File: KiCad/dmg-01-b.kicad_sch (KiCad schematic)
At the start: 64 parts, among them CN1 SCREEN, CN2 CART, CN3 EXT, CN4 AUDIO, CN5 POWER, CN6 BATTERY, P1 CART SHIELD GND PADS, P2 GND PAD, P3 GND PAD, P4 GND PAD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

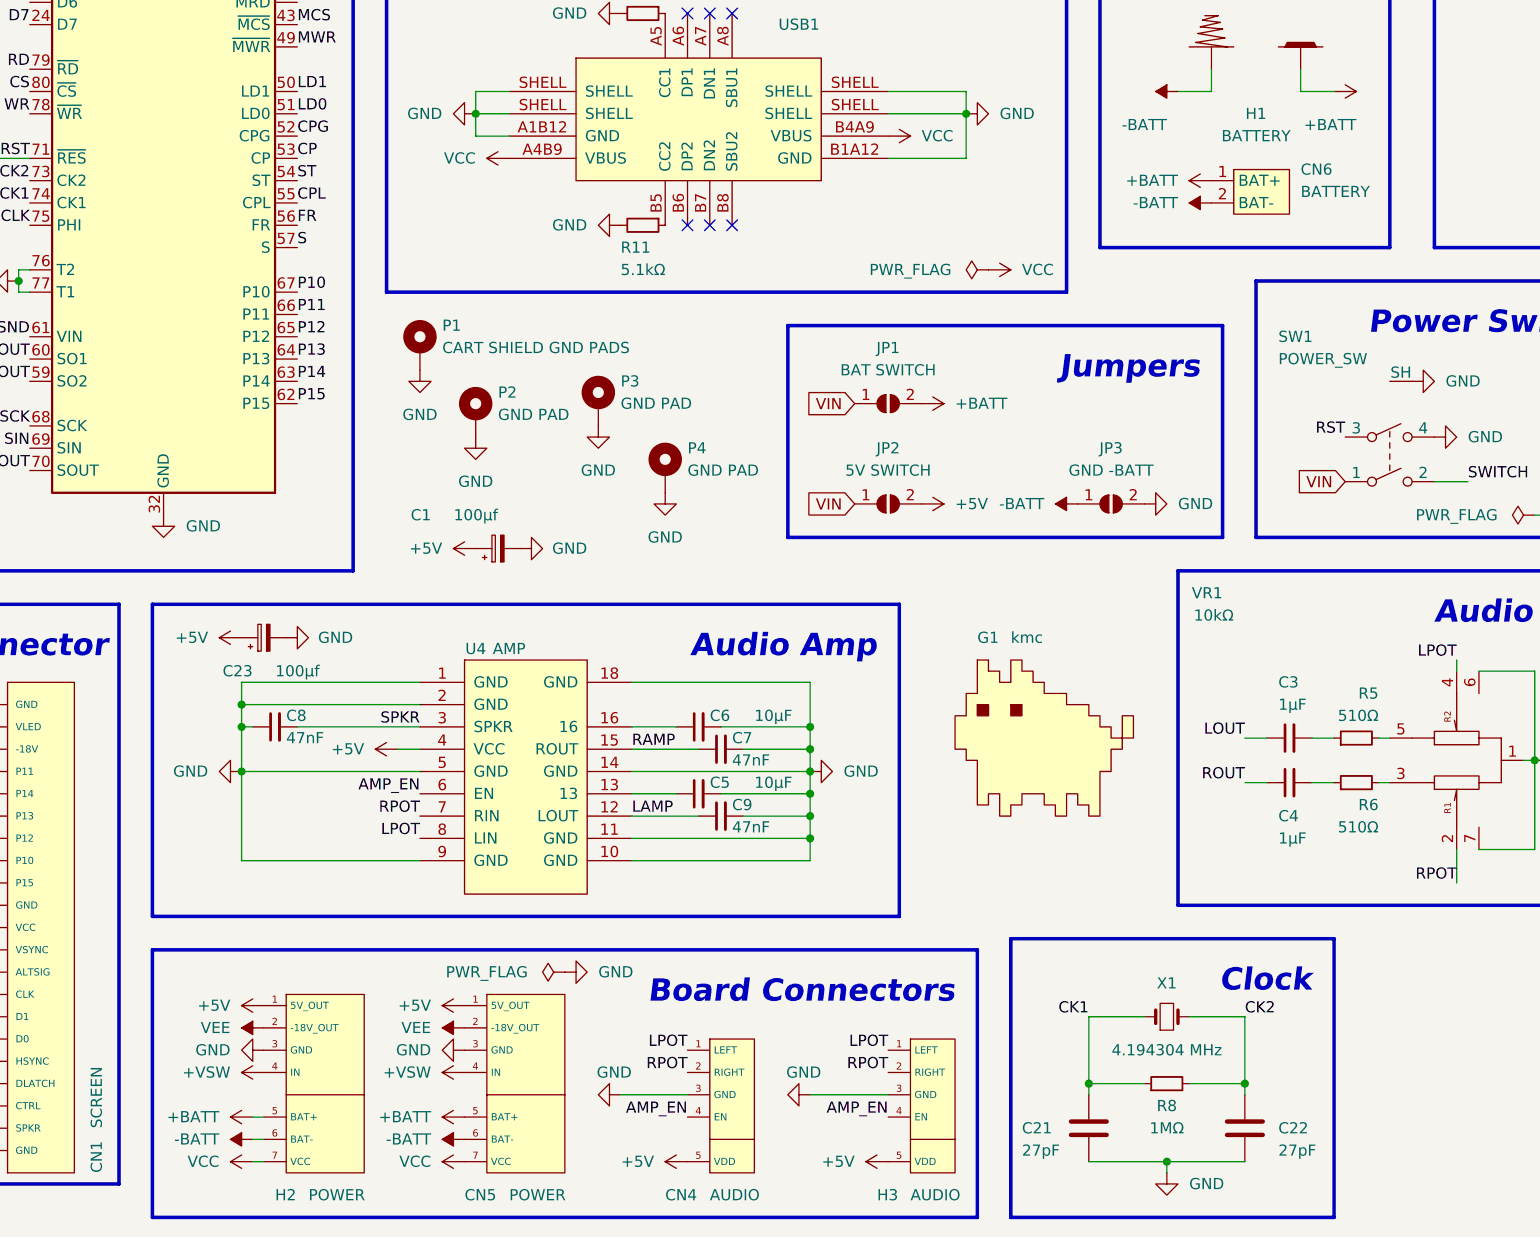
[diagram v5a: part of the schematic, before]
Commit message: fixed battery connector (!) less stupid routing in some areas minor changes
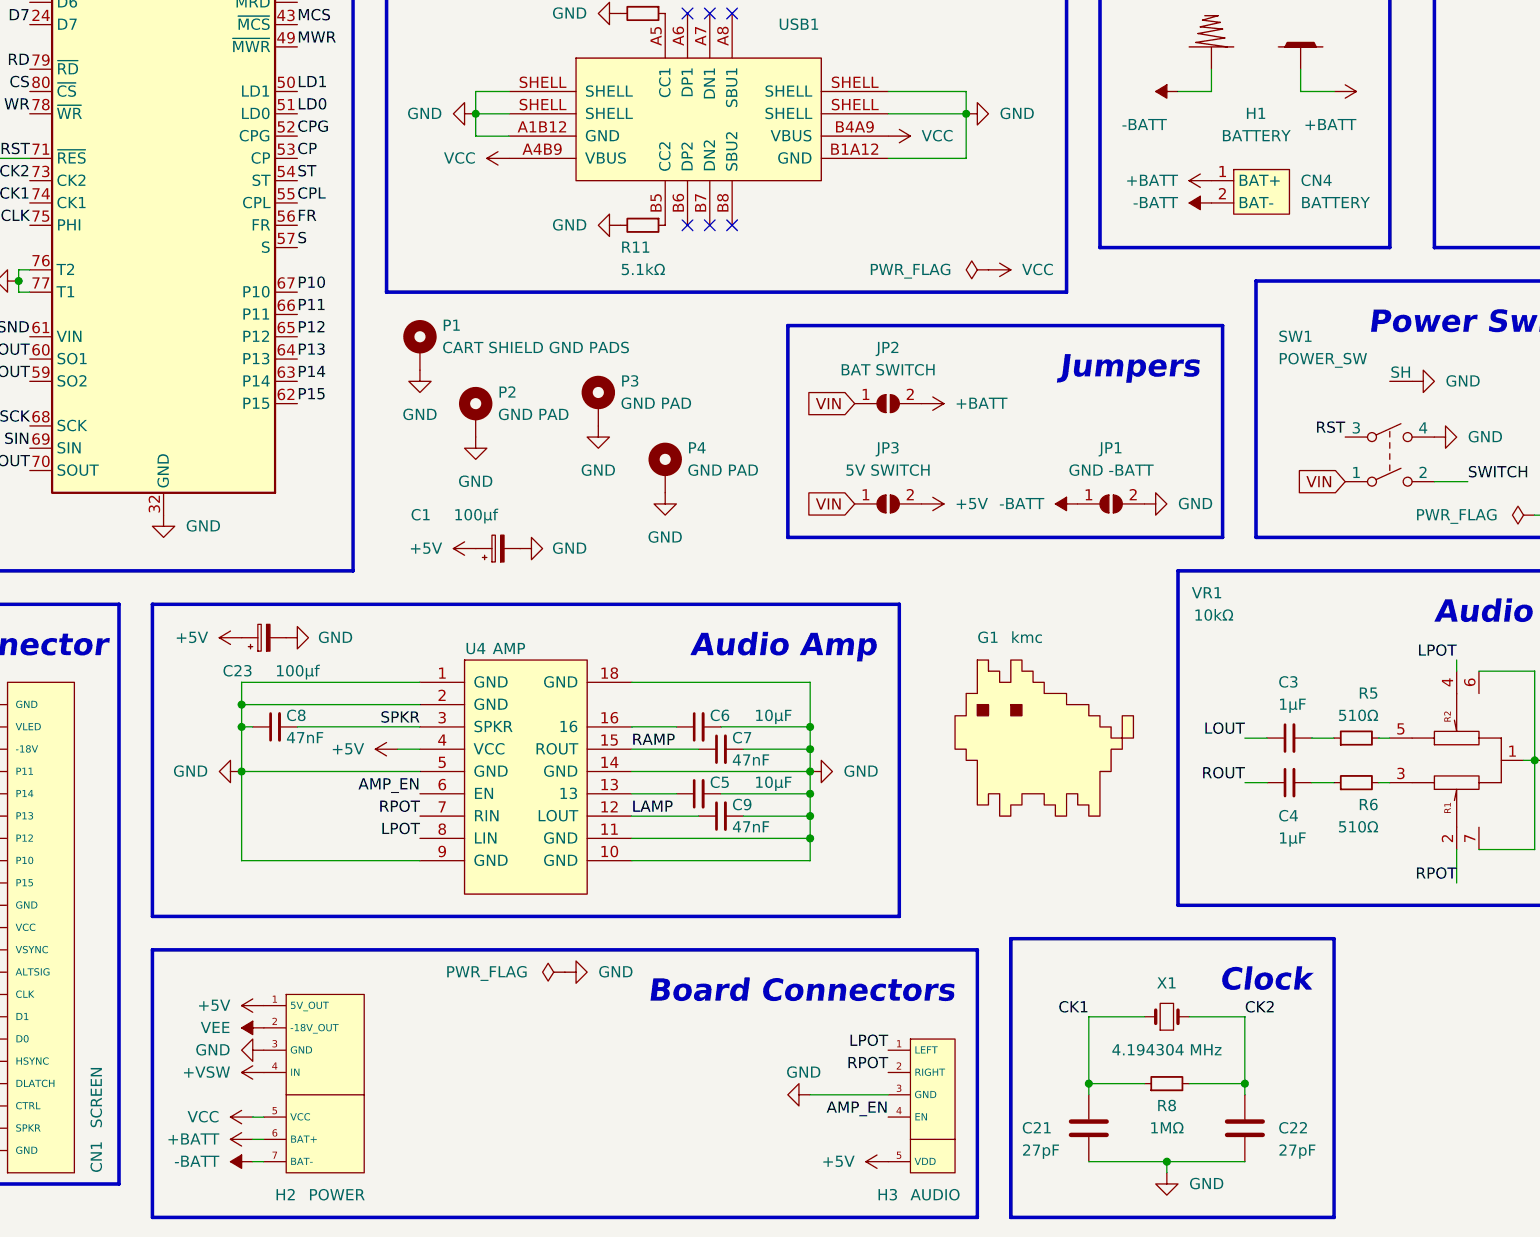
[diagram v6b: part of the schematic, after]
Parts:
- removed CN4: AUDIO, easyeda2kicad:CONN-TH_5P-P1.25_HCTL_HC-1.25-5AW, symbol kmc_lib:DMGB_AUDIO_HEADER
- removed CN5: POWER, easyeda2kicad:CONN-TH_7P-P1.25_HCTL_HC-1.25-7AW, symbol kmc_lib:DMGB_POWER_HEADER
- H1: footprint dmg_lib:DMG_BATTERY_PADS -> kmc_lib:DMG_BATTERY_PADS
- renumbered CN6 to CN4, JP3 to JP1, JP1 to JP2, JP2 to JP3
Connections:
- net +BATT: now also H1.1 (+), H2.6 (BAT+); no longer H1.2 (GND), H2.5 (BAT+)
- net -BATT: now also H1.2 (-), H2.7 (BAT-); no longer H1.1 (BAT), H2.6 (BAT-)
- net VCC: now also H2.5 (VCC); no longer H2.7 (VCC)

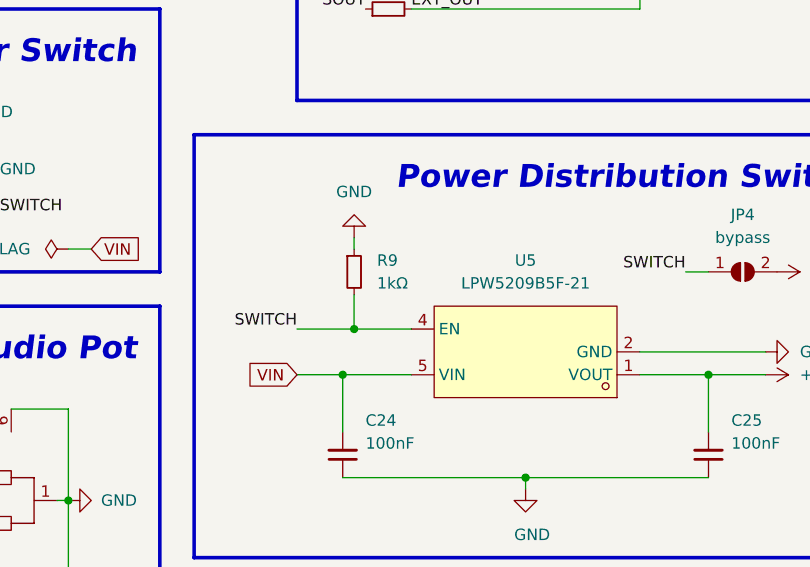
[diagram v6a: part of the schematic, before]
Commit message: add basic BOM with LCSC parts
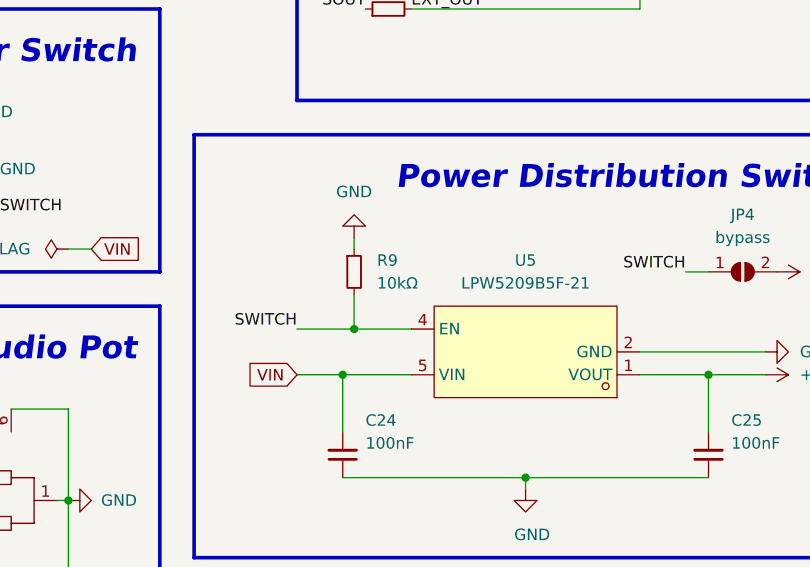
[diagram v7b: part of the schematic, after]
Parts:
- C1, C23: LCSC (none) -> C122271
- C10, C24, C25: LCSC (none) -> C49678
- C12, C13, C14: LCSC (none) -> C1710
- C16, C17, C18, C19: LCSC (none) -> C1790
- C21, C22: LCSC (none) -> C527182
- C3, C4: LCSC (none) -> C28323
- C5, C6: LCSC (none) -> C15850
- C7, C8, C9: LCSC (none) -> C53134
- CN4: JLC Part Extended Part -> (none); LCSC (none) -> C2845535; LCSC Part C2845535 -> (none)
- D2: LCSC (none) -> C83528
- DA1, DA2, DA3, DA4: LCSC (none) -> C106919; SuppliersPartNumber C106919 -> (none)
- G1, H1, H2, H3, JP4, U4: now left out of the parts list
- R1, R2, R3, R4: LCSC (none) -> C17557
- R10, R11: LCSC (none) -> C27834
- R5, R6: LCSC (none) -> C17734
- R7: LCSC (none) -> C17501
- R8: LCSC (none) -> C17514
- R9: value 1kΩ -> 10kΩ; LCSC (none) -> C17414
- U5: footprint kmc_lib:SOT-23-5_L2.9-W1.6-P0.95-LS2.8-BL -> easyeda2kicad:SOT-23-5_L2.9-W1.6-P0.95-LS2.8-BL; LCSC (none) -> C517266; LCSC Part C517266 -> (none)
- USB1: LCSC (none) -> C319148; SuppliersPartNumber C319148 -> (none)
- X1: LCSC (none) -> C2149317

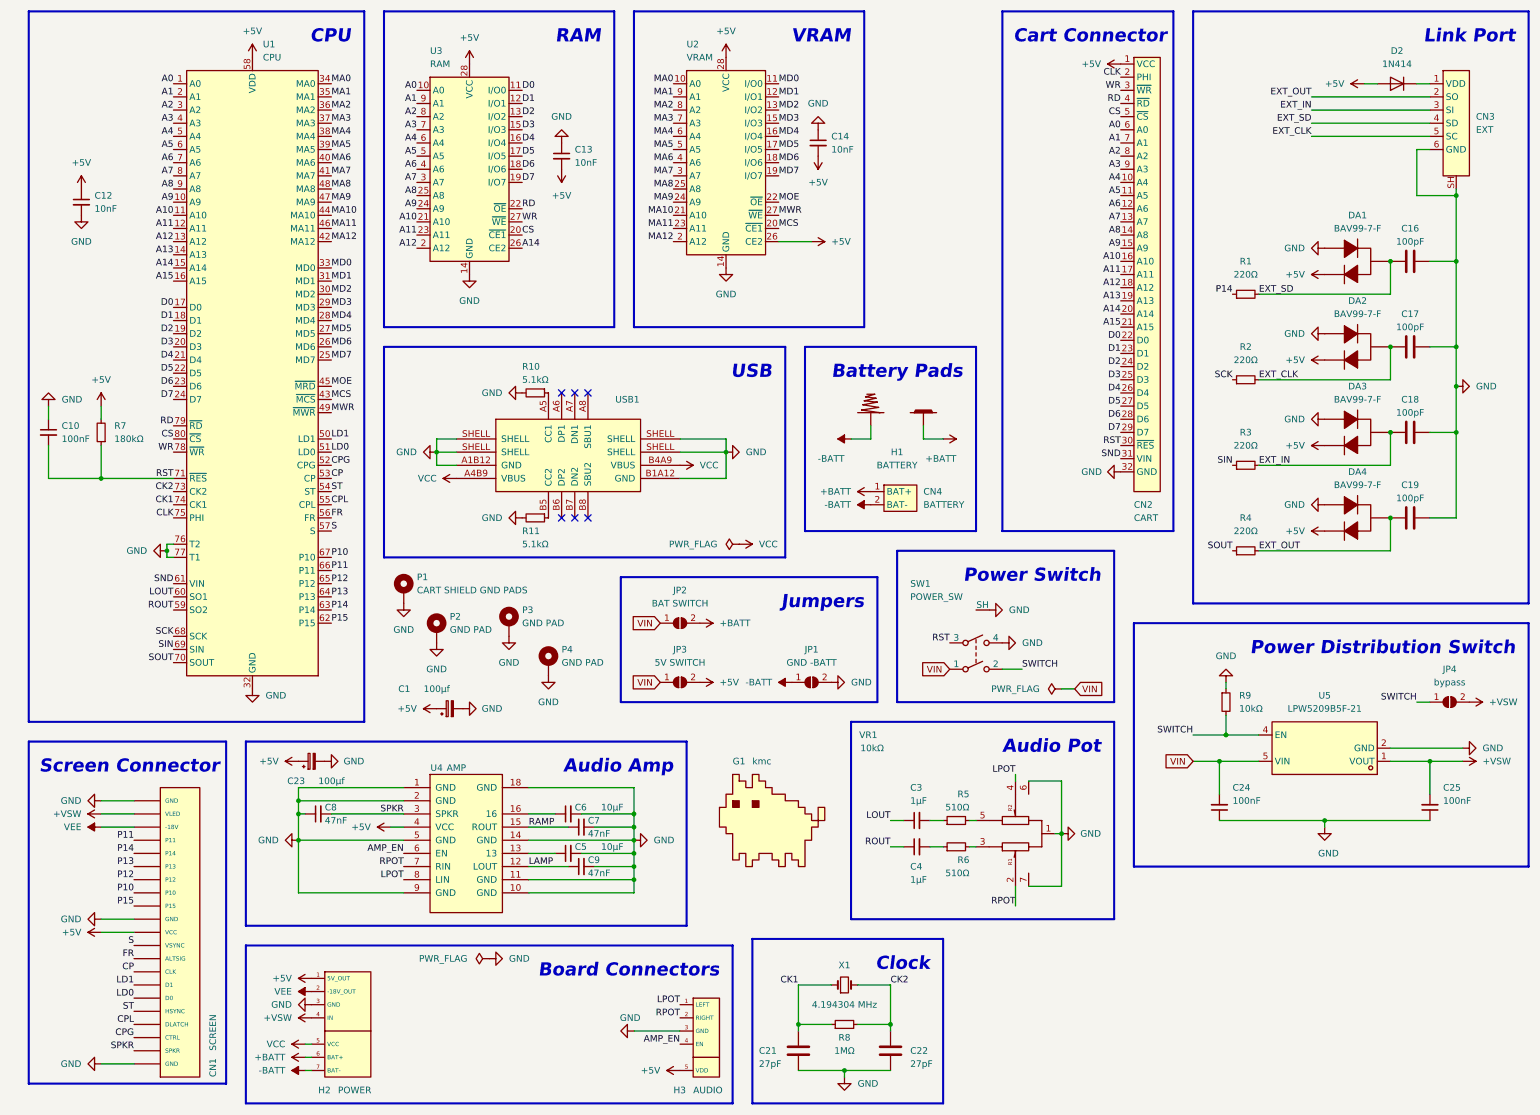
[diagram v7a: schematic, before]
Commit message: significantly simplified the power stuff
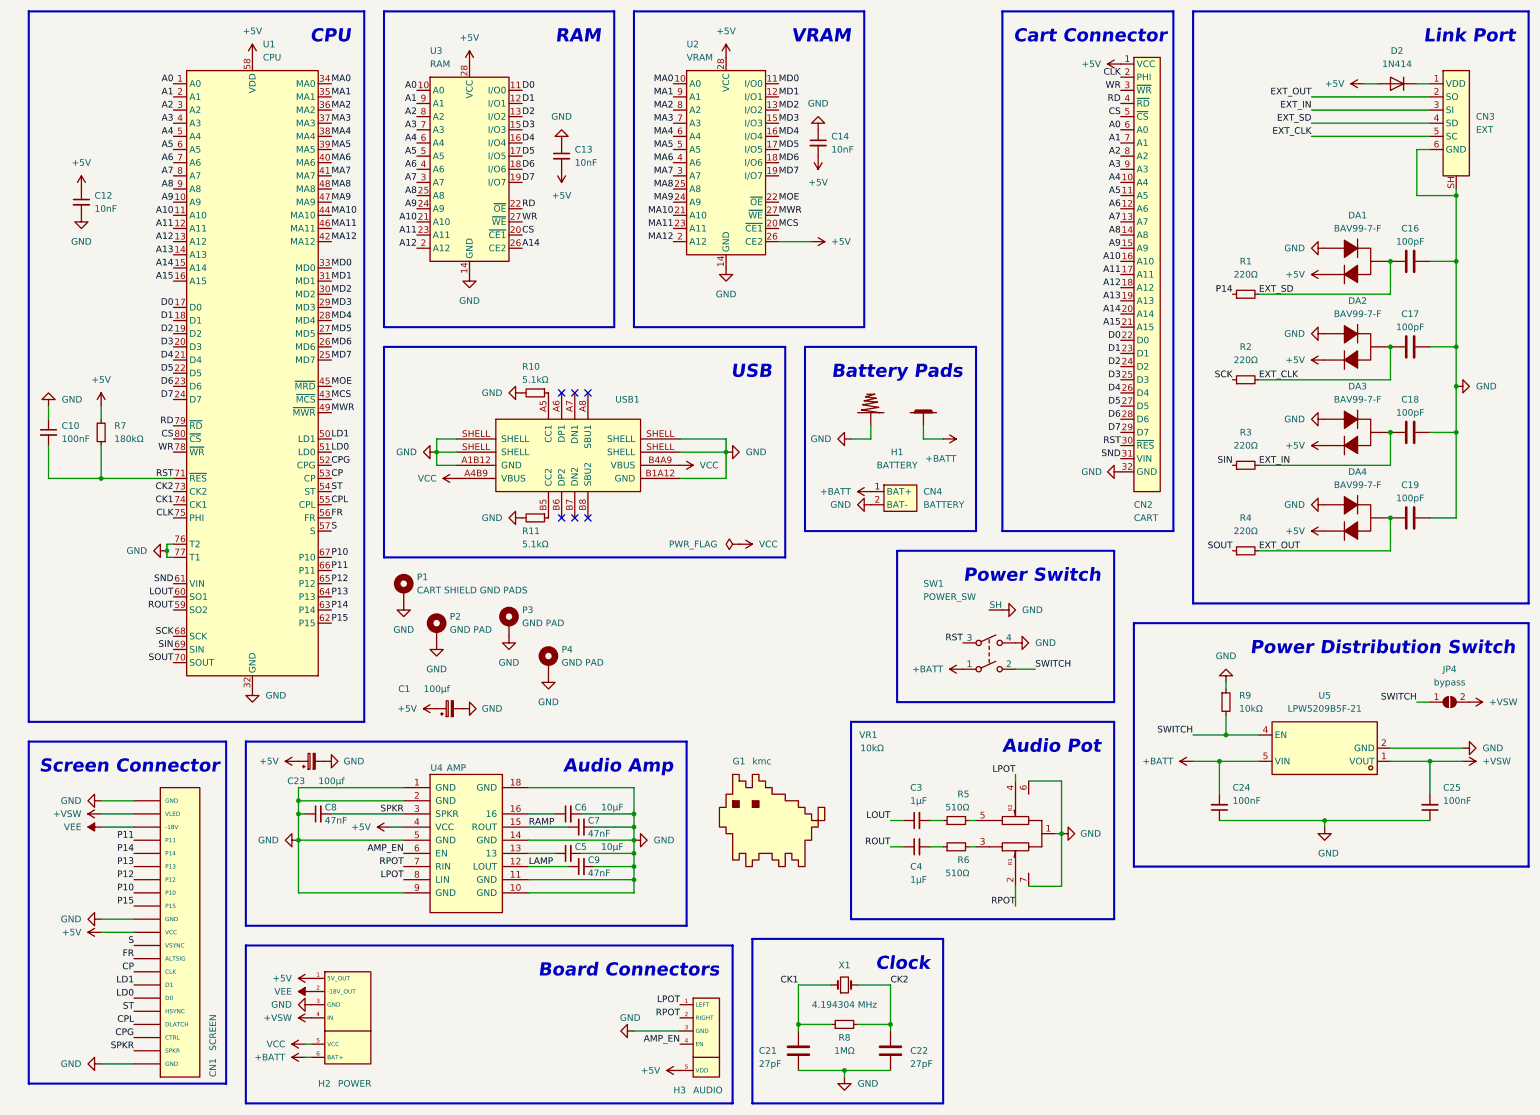
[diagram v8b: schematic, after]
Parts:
- removed JP1: GND -BATT, kmc_lib:solder_jumper_x2, symbol Jumper:SolderJumper_2_Open
- removed JP2: BAT SWITCH, kmc_lib:solder_jumper_x2, symbol Jumper:SolderJumper_2_Open
- removed JP3: 5V SWITCH, kmc_lib:solder_jumper_x2, symbol Jumper:SolderJumper_2_Open
- H2: footprint kmc_lib:2.54_PAD_SMD_X7 -> kmc_lib:2.54_PAD_SMD_X6
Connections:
- net VIN is gone; now on net +BATT: C24.2, SW1.1, U5.5 (VIN)
- net GND: now also CN4.2 (BAT-), H1.2 (-)
- removed net -BATT: CN4.2 (BAT-), H1.2 (-), H2.7 (BAT-)
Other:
- note removed: "Jumpers"
- moved on the sheet: SW1
